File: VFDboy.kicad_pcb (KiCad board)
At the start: 2 copper layers, 142 x 60 mm, 88 parts, among them J1 AVR-ISP-6, J2 USB_C_Receptacle_USB2.0, J3 Micro_SD_Card_Det, J4 TagConnect_TC2030_SWD, Q1 FS8205A, Q2 S9015, Q3 AO3401A, Q4 AO3401A, Q5 S9015, Q6 2N7002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

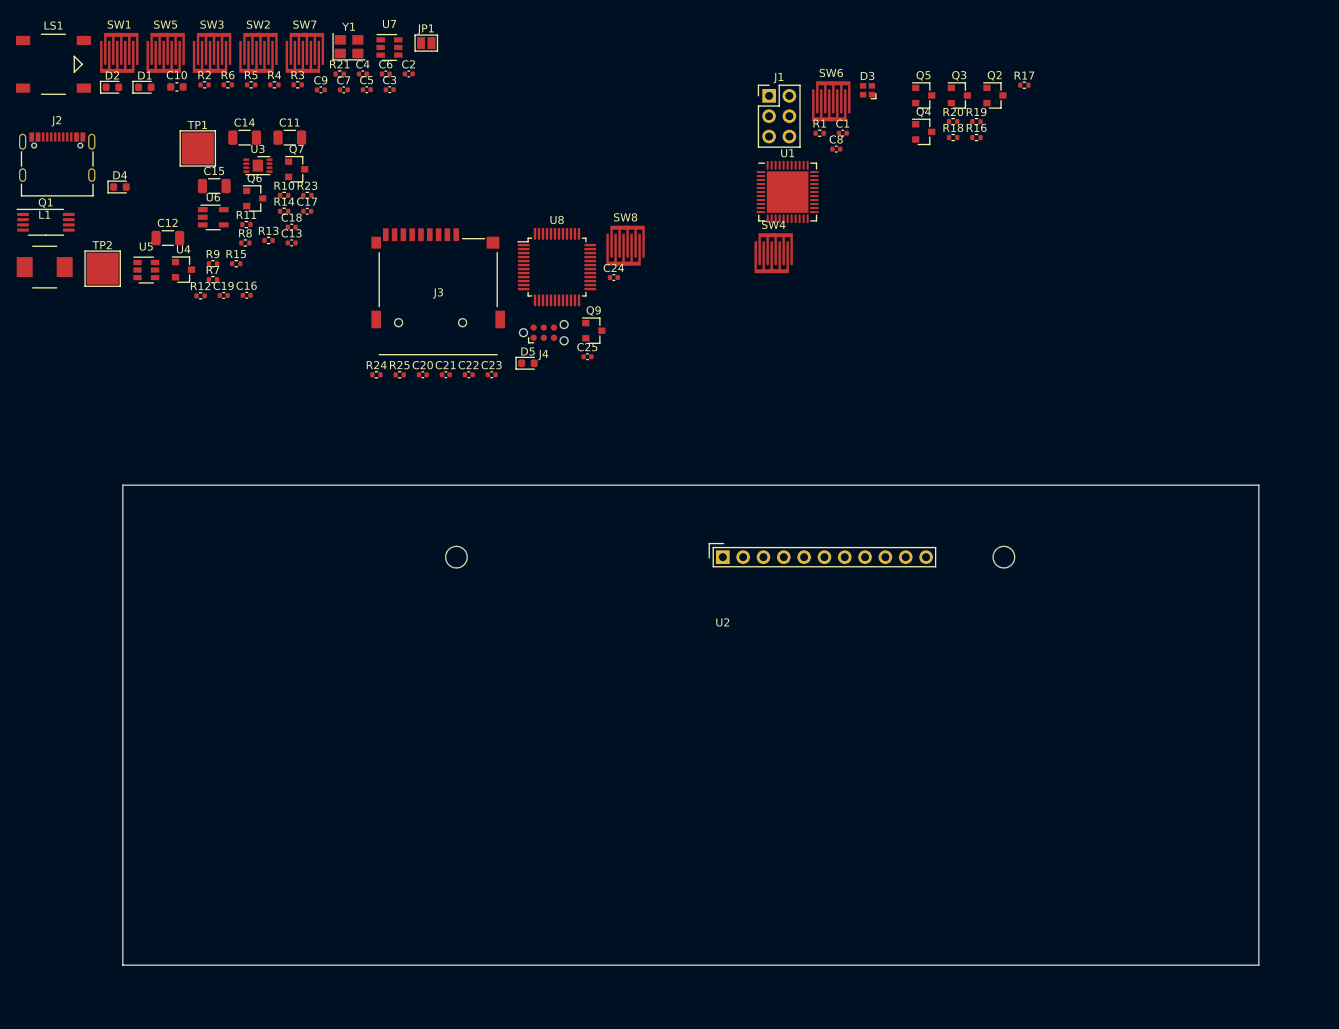
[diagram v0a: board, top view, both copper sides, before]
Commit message: Add charge state/current sensing and VBUS wakeup source
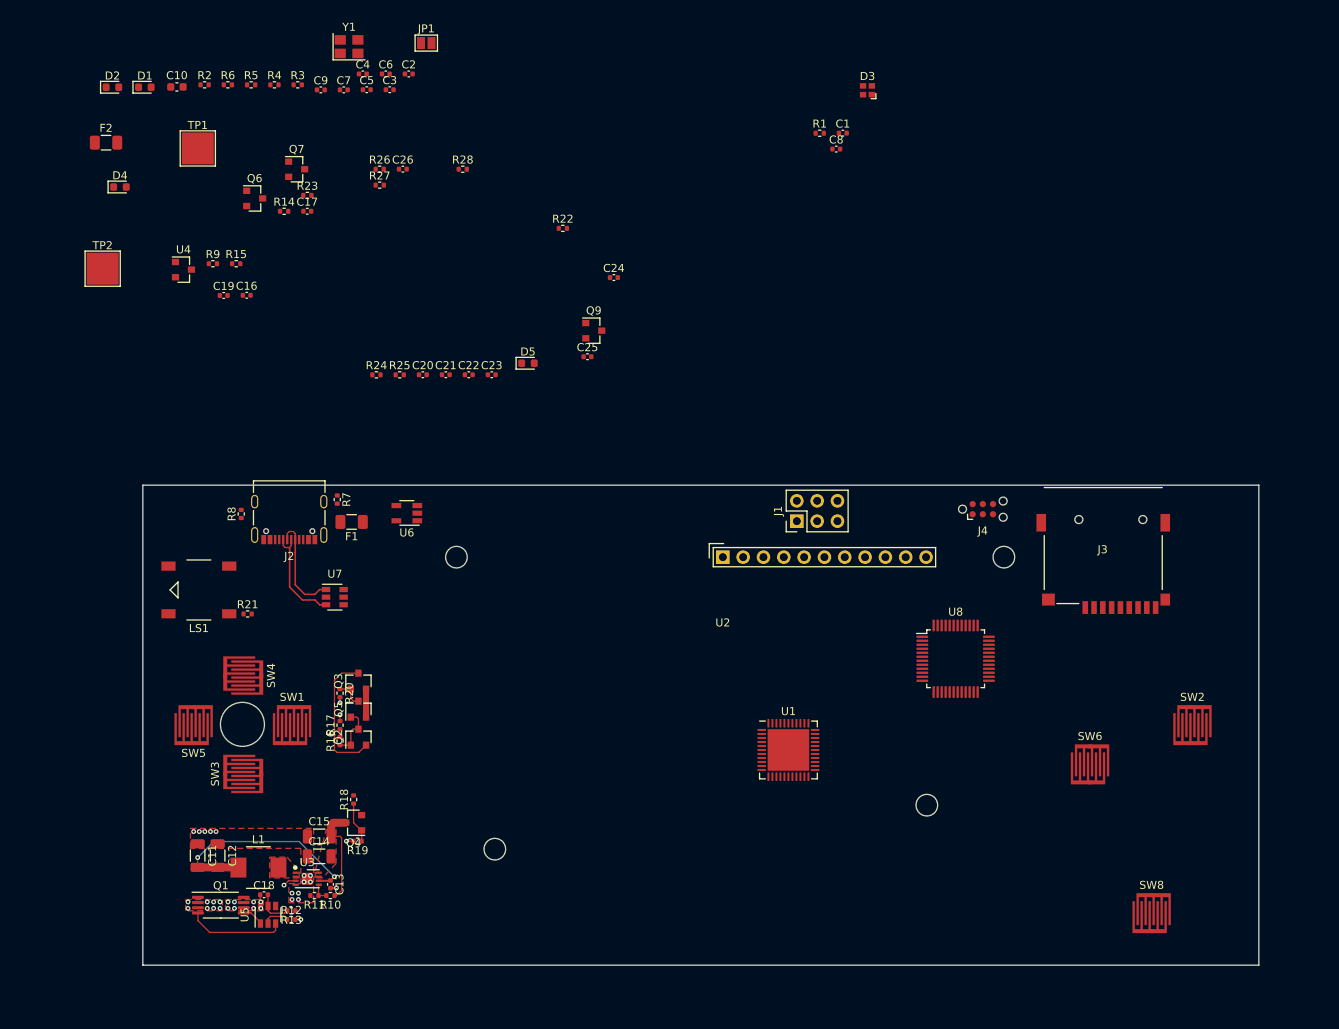
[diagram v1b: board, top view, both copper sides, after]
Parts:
- removed SW7: RESET, Button_Carbon:Button_Carbon_5mm
- added C26: 100nF, Capacitor_SMD:C_0402_1005Metric, F.Cu at (135.0, 60.5)
- added F1: Fuse, Fuse:Fuse_1206_3216Metric, F.Cu at (128.6, 104.6)
- added F2: Fuse, Fuse:Fuse_1206_3216Metric, F.Cu at (97.9, 57.2)
- added H1: DisplayStandoff, MountingHole:MountingHole_2.7mm_M2.5, F.Cu at (200.5, 140.0)
- added H2: DisplayStandoff, MountingHole:MountingHole_2.7mm_M2.5, F.Cu at (146.5, 145.5)
- added H3: D-Pad pivot, MountingHole:MountingHole_5.5mm, F.Cu at (115.0, 129.9)
- added R22: 8.2kR, Resistor_SMD:R_0402_1005Metric, F.Cu at (155.0, 67.9)
- added R26: 8.2kR, Resistor_SMD:R_0402_1005Metric, F.Cu at (132.1, 60.5)
- added R27: 8.2kR, Resistor_SMD:R_0402_1005Metric, F.Cu at (132.1, 62.5)
- added R28: 8.2kR, Resistor_SMD:R_0402_1005Metric, F.Cu at (142.5, 60.5)
- SW1: value SW_Push -> RIGHT
- SW2: value SW_Push -> A
- SW3: value SW_Push -> DOWN
- SW4: value SW_Push -> UP
- SW5: value SW_Push -> LEFT
- SW6: value SW_Push -> B
- moved SW2 143.8 mm to (233.7, 130.0)
- moved R19 118.6 mm to (129.3, 144.5), turned to 180 degrees
- moved R17 117.1 mm to (127.2, 130.0), turned to 90 degrees
- moved Q2 113.0 mm to (129.4, 131.5), turned to 90 degrees
- moved Q4 112.0 mm to (128.8, 142.2), turned to 180 degrees
- moved R18 111.6 mm to (128.8, 139.3), turned to 90 degrees
- moved R16 109.6 mm to (127.2, 132.0), turned to 90 degrees
- moved SW8 106.2 mm to (228.6, 153.5)
- moved Q3 104.9 mm to (129.4, 124.5), turned to 90 degrees
- moved R20 104.8 mm to (127.2, 126.0), turned to 270 degrees
- moved Q5 104.3 mm to (129.4, 128.0), turned to 90 degrees
- moved J3 96.2 mm to (227.5, 104.3), turned to 180 degrees
- moved C11 90.5 mm to (109.3, 146.3), turned to 270 degrees
- moved C14 90.3 mm to (124.5, 146.4)
- moved SW3 90.2 mm to (115.0, 136.1), turned to 270 degrees
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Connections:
- D4 pad 1: Net-(D4-Pad1) -> /Power/LEDchg
- J2 pad A4: VBUS -> Net-(F1-Pad2)
- J2 pad A9: VBUS -> Net-(F1-Pad2)
- J2 pad B4: VBUS -> Net-(F1-Pad2)
- J2 pad B9: VBUS -> Net-(F1-Pad2)
- TP1 pad 1: +BATT -> Net-(F2-Pad2)
- U6 pad 1: Net-(D4-Pad1) -> /Power/LEDchg
- U8 pad 13: Net-(U8-Pad13) -> /Power/Ichg
- U8 pad 20: Net-(U8-Pad20) -> /Power/LEDchg
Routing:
- net +BATT: track 0.00 -> 28.2 mm, vias 0 -> 2
- net /Power/Power switch/VUSB: track 0.00 -> 16.5 mm
- net /D+: track 0.00 -> 13.1 mm
- net /D-: track 0.00 -> 12.9 mm
- net Net-(Q1-Pad4): track 0.00 -> 12.2 mm
- net /Power/Power switch/VSTEP_UP: track 0.00 -> 12.1 mm
- net Net-(Q2-Pad1): track 0.00 -> 6.49 mm
- net Net-(Q4-Pad1): track 0.00 -> 5.20 mm
- net Net-(C18-Pad2): track 0.00 -> 4.74 mm
- net Net-(Q3-Pad1): track 0.00 -> 3.89 mm
- net GND: track 0.00 -> 3.82 mm, vias 0 -> 26
- net +5V: track 0.00 -> 3.50 mm
- net Net-(R12-Pad1): track 0.00 -> 3.29 mm
- net Net-(Q1-Pad5): track 0.00 -> 2.70 mm
- net Net-(R10-Pad2): track 0.00 -> 2.39 mm
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- added copper zone on F.Cu, net /Power/Power switch/VSTEP_UP
- added copper zone on F.Cu, net GND
- added copper zone on F.Cu, net Net-(C18-Pad1)
- added copper zone on F.Cu, net Net-(L1-Pad2)
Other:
- board size 142 x 60 mm -> 139.5 x 60 mm
- board text added: "Filament transformers"
- board text added: "High EMI!"
- board text added: "Speaker ramp"
- board text added: "USB"

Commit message: Implement fuel gauging
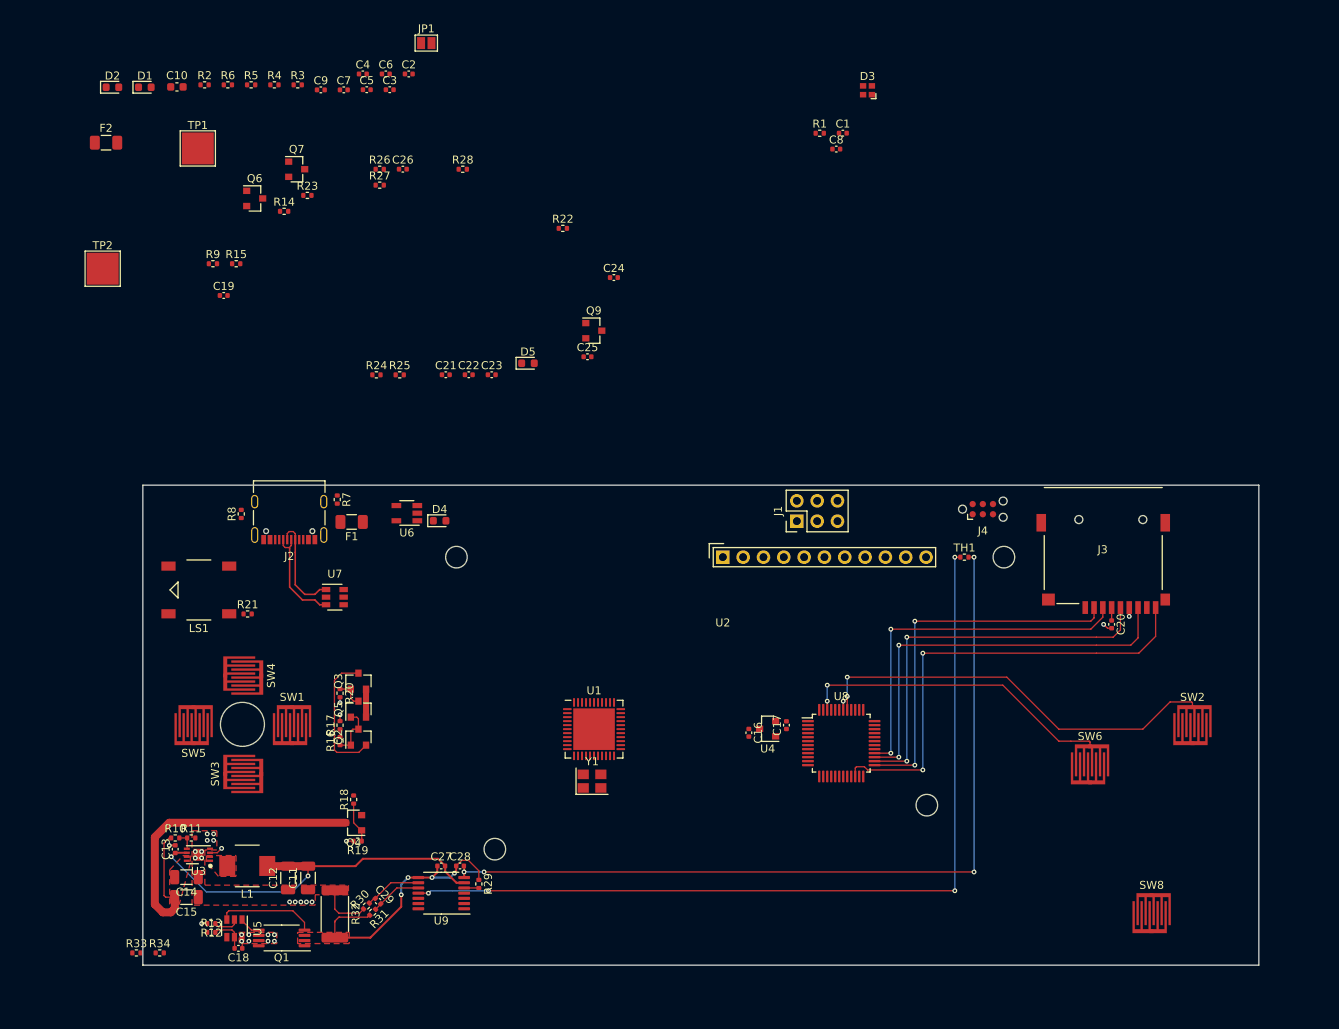
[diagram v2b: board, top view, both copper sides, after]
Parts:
- added C27: 100nF, Capacitor_SMD:C_0402_1005Metric, F.Cu at (139.8, 147.6)
- added C28: 1uF, Capacitor_SMD:C_0402_1005Metric, F.Cu at (142.2, 147.6)
- added C29: 100nF, Capacitor_SMD:C_0402_1005Metric, F.Cu at (131.9, 152.0)
- added R29: 1MR, Resistor_SMD:R_0402_1005Metric, F.Cu at (144.5, 149.8)
- added R30: 100R, Resistor_SMD:R_0402_1005Metric, F.Cu at (130.4, 152.6)
- added R31: 100R, Resistor_SMD:R_0402_1005Metric, F.Cu at (131.2, 153.4)
- added R32: 25mR, Resistor_SMD:R_2512_6332Metric, F.Cu at (126.5, 153.6)
- added R33: 3.3kR, Resistor_SMD:R_0402_1005Metric, F.Cu at (101.7, 158.5)
- added R34: 3.3kR, Resistor_SMD:R_0402_1005Metric, F.Cu at (104.6, 158.5)
- added TH1: 10kR 3380K, Resistor_SMD:R_0402_1005Metric, F.Cu at (205.2, 109.0)
- added U9: BQ34Z100, Package_SO:TSSOP-14_4.4x5mm_P0.65mm, F.Cu at (139.8, 151.0)
- moved Y1 96.7 mm to (158.7, 137.0)
- moved U4 92.9 mm to (180.6, 130.4), turned to 180 degrees
- moved C20 91.6 mm to (223.6, 117.4), turned to 270 degrees
- moved C17 87.8 mm to (182.9, 130.0), turned to 90 degrees
- moved C16 83.2 mm to (178.2, 130.9), turned to 270 degrees
- moved D4 57.8 mm to (139.6, 104.5)
- moved U1 24.4 mm to (158.9, 130.5)
- moved R10 20.7 mm to (106.5, 144.1), turned to 0 degrees
- moved C13 19.9 mm to (106.5, 145.5), turned to 90 degrees
- moved C15 18.3 mm to (108.0, 151.5), turned to 180 degrees
- moved U8 17.8 mm to (189.8, 132.2)
- moved R11 17.0 mm to (108.5, 144.1), turned to 0 degrees
- moved C14 16.8 mm to (108.0, 149.0), turned to 180 degrees
- moved C11 14.1 mm to (123.2, 149.1), turned to 90 degrees
- moved U3 13.9 mm to (109.5, 146.2), turned to 180 degrees
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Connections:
- Q1 pad 2: GND -> GNDREF
- Q1 pad 3: GND -> GNDREF
- SW1 pad 1: Net-(SW1-Pad1) -> /RIGHT
- SW2 pad 1: Net-(SW2-Pad1) -> /A
- SW3 pad 1: Net-(SW3-Pad1) -> /DOWN
- SW4 pad 2: Net-(SW4-Pad2) -> /UP
- SW5 pad 1: Net-(SW5-Pad1) -> /LEFT
- SW6 pad 1: Net-(SW6-Pad1) -> /B
- U1 pad 1: Net-(SW2-Pad1) -> /A
- U1 pad 28: Net-(SW6-Pad1) -> /B
- U1 pad 36: Net-(SW4-Pad2) -> /UP
- U1 pad 37: Net-(SW1-Pad1) -> /RIGHT
- U1 pad 38: Net-(SW5-Pad1) -> /LEFT
- U1 pad 39: Net-(SW3-Pad1) -> /DOWN
- U8 pad 21: Net-(U8-Pad21) -> /UP
- U8 pad 32: Net-(U8-Pad32) -> /DOWN
- U8 pad 33: Net-(U8-Pad33) -> /RIGHT
- U8 pad 38: Net-(U8-Pad38) -> /LEFT
- U8 pad 41: Net-(U8-Pad41) -> /A
- U8 pad 42: Net-(U8-Pad42) -> /Power/SCL
- U8 pad 43: Net-(U8-Pad43) -> /Power/SDA
- U8 pad 45: Net-(U8-Pad45) -> /Power/GAUGE_EN
- U8 pad 46: Net-(U8-Pad46) -> /B
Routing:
- net Net-(TH1-Pad1): track 0.00 -> 109.6 mm, vias 0 -> 4
- net Net-(C28-Pad2): track 0.00 -> 105.4 mm, vias 0 -> 4
- net Net-(J3-Pad10): track 0.00 -> 57.9 mm, vias 0 -> 2
- net /A: track 0.00 -> 51.9 mm, vias 0 -> 2
- net Net-(J3-Pad7): track 0.00 -> 51.1 mm, vias 0 -> 2
- net Net-(J3-Pad5): track 0.00 -> 49.4 mm, vias 0 -> 2
- net Net-(J3-Pad2): track 0.00 -> 46.9 mm, vias 0 -> 2
- net Net-(J3-Pad3): track 0.00 -> 45.9 mm, vias 0 -> 2
- net /B: track 0.00 -> 39.4 mm, vias 0 -> 2
- net /Power/Power switch/VSTEP_UP: track 12.1 -> 46.4 mm
- net GNDREF: track 0.00 -> 34.2 mm, vias 0 -> 4
- net +BATT: track 28.2 -> 49.7 mm
- net GND: track 3.82 -> 12.5 mm, vias 26 -> 20
- net Net-(C29-Pad1): track 0.00 -> 7.18 mm
- net Net-(C29-Pad2): track 0.00 -> 6.45 mm
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- added copper zone on F.Cu, net GNDREF

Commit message: Partially routed
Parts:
- moved R25 108.4 mm to (225.8, 144.7)
- moved D5 101.4 mm to (232.5, 144.6)
- moved C10 87.3 mm to (162.0, 117.8), turned to 270 degrees
- moved R24 81.8 mm to (208.8, 113.5), turned to 270 degrees
- moved C2 81.0 mm to (150.8, 128.2), turned to 90 degrees
- moved R1 80.7 mm to (148.2, 126.7)
- moved C9 80.0 mm to (152.5, 125.6)
- moved C1 79.6 mm to (156.4, 128.2), turned to 90 degrees
- moved C3 78.4 mm to (149.7, 127.2), turned to 90 degrees
- moved R28 77.6 mm to (179.2, 128.9), turned to 90 degrees
- moved C4 73.9 mm to (148.1, 120.2), turned to 180 degrees
- moved C5 69.6 mm to (148.2, 117.9)
- moved C23 69.5 mm to (192.0, 138.4), turned to 90 degrees
- moved C24 65.1 mm to (195.6, 129.4), turned to 90 degrees
- moved Q7 62.8 mm to (129.4, 122.8), turned to 270 degrees
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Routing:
- net /RIGHT: track 0.00 -> 193.4 mm, vias 0 -> 8
- net /DOWN: track 0.00 -> 173.3 mm, vias 0 -> 9
- net /UP: track 0.00 -> 165.2 mm, vias 0 -> 8
- net /LEFT: track 0.00 -> 157.8 mm, vias 0 -> 9
- net /MOSI: track 0.00 -> 147.4 mm, vias 0 -> 10
- net /Power/SCL: track 1.09 -> 142.2 mm, vias 1 -> 6
- net /Power/SDA: track 0.00 -> 129.4 mm, vias 0 -> 6
- net /Power/GAUGE_EN: track 1.84 -> 120.0 mm, vias 0 -> 4
- net /MISO: track 0.00 -> 116.0 mm, vias 0 -> 6
- net /~RST: track 0.00 -> 106.5 mm, vias 0 -> 5
- net /SCK: track 0.00 -> 100.9 mm, vias 0 -> 7
- net /~OLEDRST: track 0.00 -> 91.3 mm, vias 0 -> 4
- net /~CS: track 0.00 -> 85.1 mm, vias 0 -> 5
- net /~DC: track 0.00 -> 76.8 mm, vias 0 -> 6
- net +3V3: track 0.00 -> 67.8 mm, vias 0 -> 2
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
